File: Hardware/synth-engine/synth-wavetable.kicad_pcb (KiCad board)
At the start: 2 copper layers, 100 x 100 mm, 143 parts, among them J1 SWD_programming, J2 USB-B-S, J3 MIDI_IN, J4 MIDI_OUT, J5 SWD_JTAG, J7 POWER_JACKPTH, J8 Conn_02x12_Odd_Even, Q1 2N3904, U1 CY8C4246AZI-L445, U10 NJM4580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

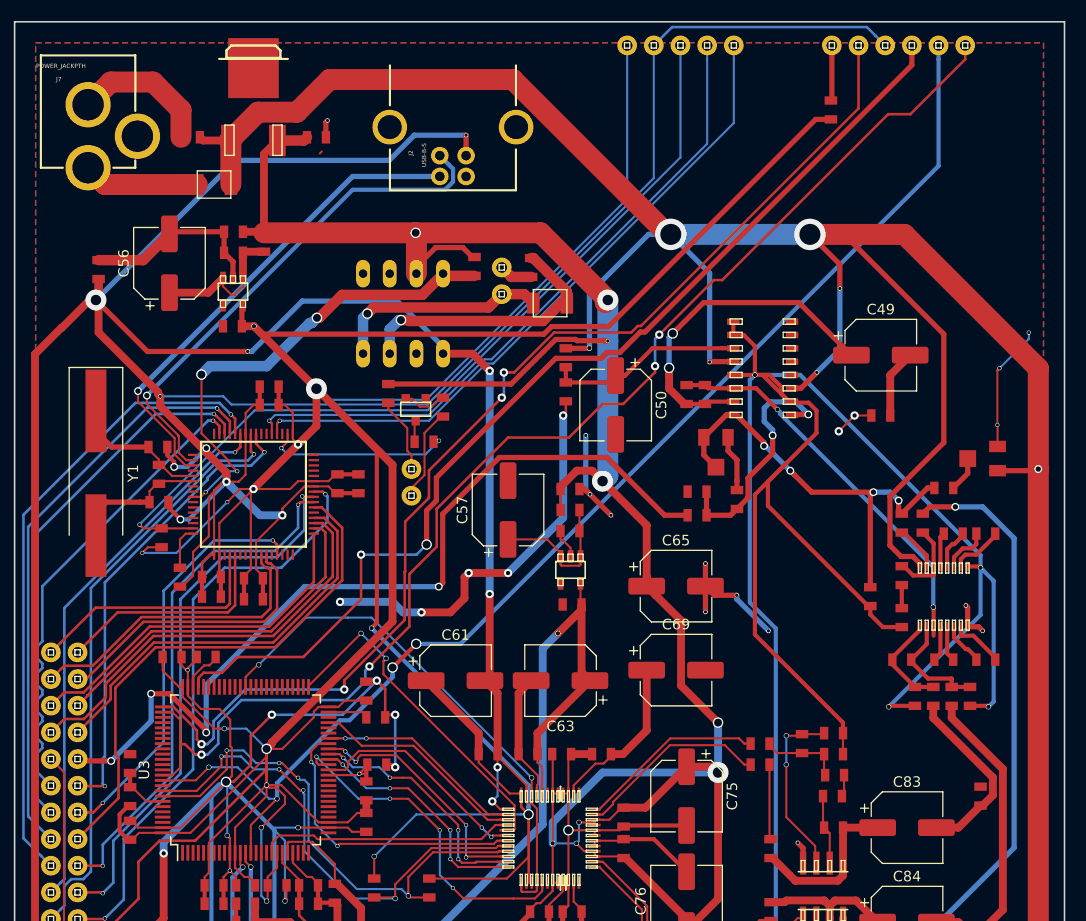
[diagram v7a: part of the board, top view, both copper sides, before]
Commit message: fix some footprint errors
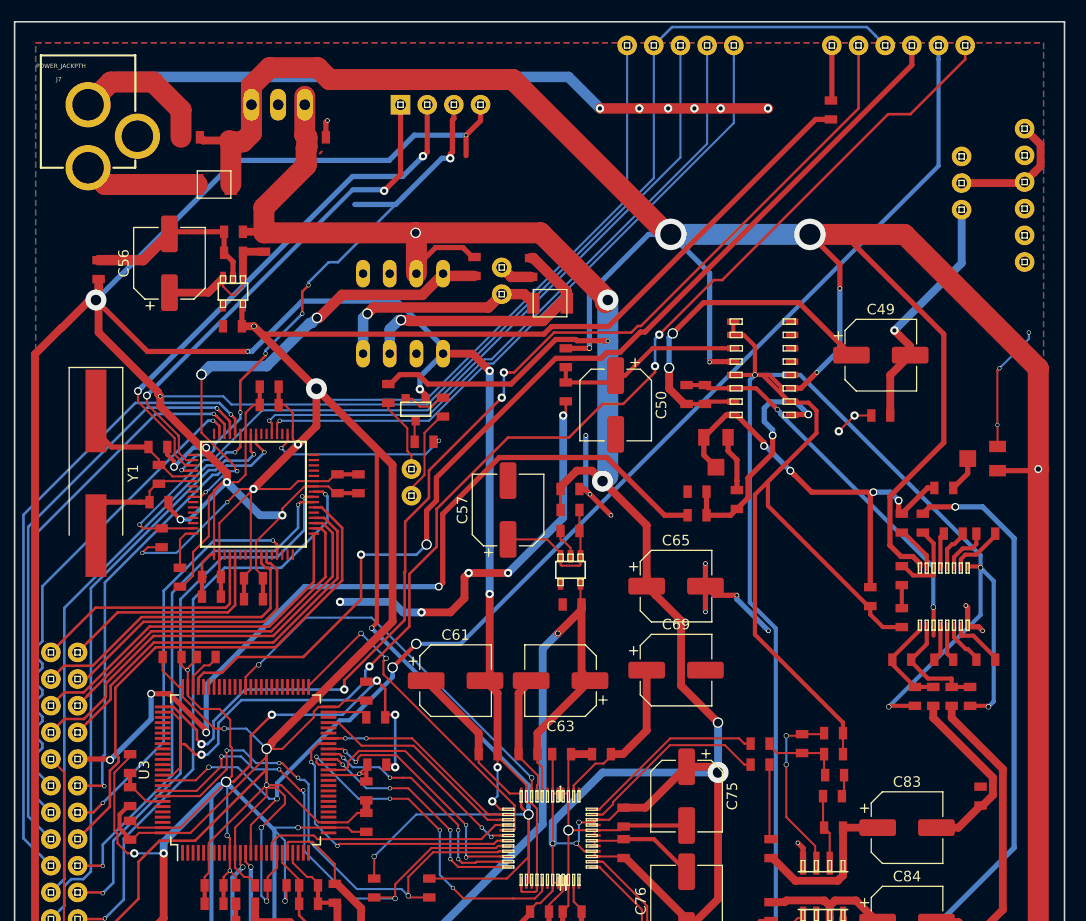
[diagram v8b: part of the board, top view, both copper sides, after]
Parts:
- added J6: Conn_01x03, SparkFun-Connectors:1X03, F.Cu at (90.2, 17.9)
- added J9: Conn_01x06, SparkFun-Connectors:1X06, F.Cu at (96.2, 10.2)
- J2: value USB-B-S -> Conn_01x04; footprint SparkFun-Connectors:USB-B-PTH -> SparkFun-Connectors:1X04; moved to F.Cu
- U6: footprint SparkFun-DiscreteSemi:DPAK -> SparkFun-DiscreteSemi:TO220V
- moved J2 6.96 mm to (36.8, 7.90), turned to 0 degrees
- moved U6 3.02 mm to (25.1, 7.90)
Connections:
- U1 pad 34: Net-(J2-PadD+) -> Net-(J2-Pad1)
- U1 pad 35: Net-(J2-PadD-) -> Net-(J2-Pad2)
- U1 pad 36: Net-(J2-PadVUSB) -> VBUS
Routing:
- net GND: track 233.6 -> 300.7 mm, vias 25 -> 31
- net VBUS: track 0.00 -> 53.6 mm, vias 0 -> 6
- net Net-(J2-Pad2): track 0.00 -> 51.2 mm, vias 0 -> 2
- net Net-(J2-PadD+): track 49.0 -> 0.00 mm, vias 1 -> 0
- net Net-(J2-Pad1): track 0.00 -> 48.0 mm, vias 0 -> 2
- net Net-(J2-PadD-): track 46.9 -> 0.00 mm, vias 1 -> 0
- net GNDD: track 577.5 -> 600.5 mm, vias 26 -> 28
- net Net-(C49-Pad2): track 6.54 -> 23.7 mm, vias 0 -> 1
- net Net-(J6-Pad2): track 0.00 -> 12.4 mm
- net +5V: track 239.4 -> 243.1 mm
- net +15V: track 275.5 -> 279.0 mm
